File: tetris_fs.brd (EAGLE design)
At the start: 80.9 x 50.8 mm, 20 parts, among them IC1 78L24Z, U1 328P, Y1 16MHz

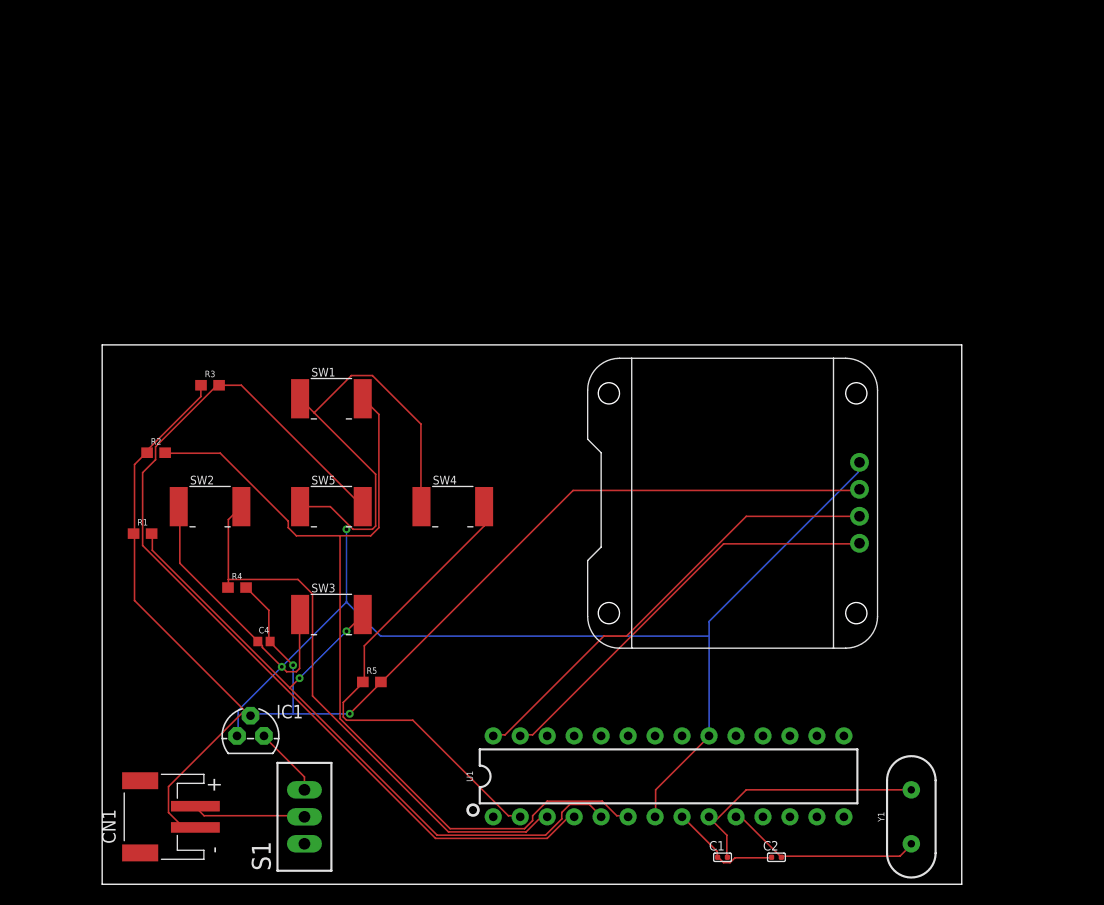
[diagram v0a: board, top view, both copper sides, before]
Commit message: Added full size resistor/capacitor version
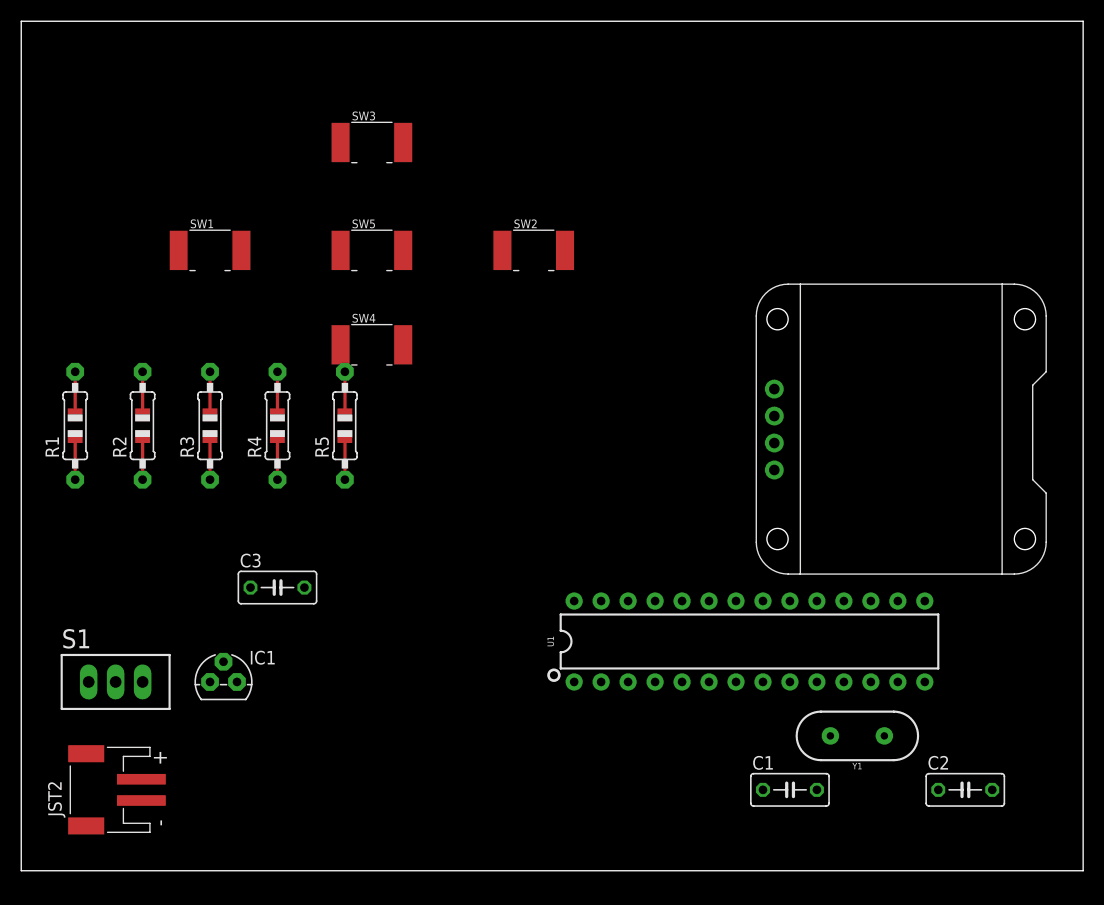
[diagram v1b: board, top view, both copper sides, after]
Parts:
- removed C4: 0.1uF, SparkFun-Capacitors:0402
- removed CN1: (no value), adafruit:JST-PH-2-SMT-RA
- added C3: 0.1uF, adafruit:C050-030X075
- added JST2: 1000mah 5V, adafruit:JST-PH-2-SMT-RA
- C1, C2: device Seeed-Capacitor:C0402 -> adafruit:C050-030X075
- R1, R2, R3, R4, R5: value 4.7k -> 1k; device SparkFun-Resistors:0603 -> adafruit:0805-THM
- moved SW3 44.6 mm to (33.0, 68.6)
- moved SW2 38.9 mm to (48.3, 58.4)
- moved SW5 24.4 mm to (33.0, 58.4)
- moved R5 24.3 mm to (30.5, 41.9), turned to 90 degrees
- moved FRAME1 22.2 mm to (-26.7, 74.9)
- moved S1 21.8 mm to (8.89, 17.8), turned to 0 degrees
- moved C2 18.9 mm to (88.9, 7.62), turned to 0 degrees
- moved SW1 18.1 mm to (17.8, 58.4)
- moved SW4 17.0 mm to (33.0, 49.5)
- moved U$1 17.0 mm to (82.5, 41.9), turned to 90 degrees
- moved R4 15.7 mm to (24.1, 41.9), turned to 90 degrees
- moved U1 14.8 mm to (68.6, 21.6)
- moved R1 12.0 mm to (5.08, 41.9), turned to 90 degrees
- moved Y1 9.16 mm to (78.7, 12.7), turned to 180 degrees
- moved C1 8.98 mm to (72.4, 7.62), turned to 0 degrees
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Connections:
- net GND: now also C3.2, JST2.2, R1.2, R2.2, R3.2; no longer C4.2, CN1.2, R1.1, R2.1, R3.1
- net N$1: no longer R2.2
- net N$2: now also R1.1; no longer R1.2
- net N$3: now also R3.1, R5.1; no longer R3.2
- net N$4: now also R2.1; no longer R4.1
- net N$5: now also R4.1; no longer R5.1
- net N$9: now also JST2.1; no longer CN1.1
- net VCC: now also C3.1; no longer C4.1
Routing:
- net VCC: track 171.6 -> 0.00 mm, vias 2 -> 0
- net GND: track 134.8 -> 0.00 mm, vias 2 -> 0
- net N$3: track 89.3 -> 0.00 mm
- net N$1: track 87.5 -> 0.00 mm
- net N$2: track 66.8 -> 0.00 mm, vias 2 -> 0
- net N$4: track 54.3 -> 0.00 mm
- net N$5: track 45.9 -> 0.00 mm
- net N$11: track 43.1 -> 0.00 mm
- net N$10: track 39.5 -> 0.00 mm
- net N$6: track 25.1 -> 0.00 mm
- net N$7: track 18.7 -> 0.00 mm
- net N$9: track 10.8 -> 0.00 mm
- net N$8: track 10.7 -> 0.00 mm
- net N$12: track 6.66 -> 0.00 mm
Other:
- board size 80.9 x 50.8 mm -> 100 x 80 mm

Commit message: updated board layout, updated readme
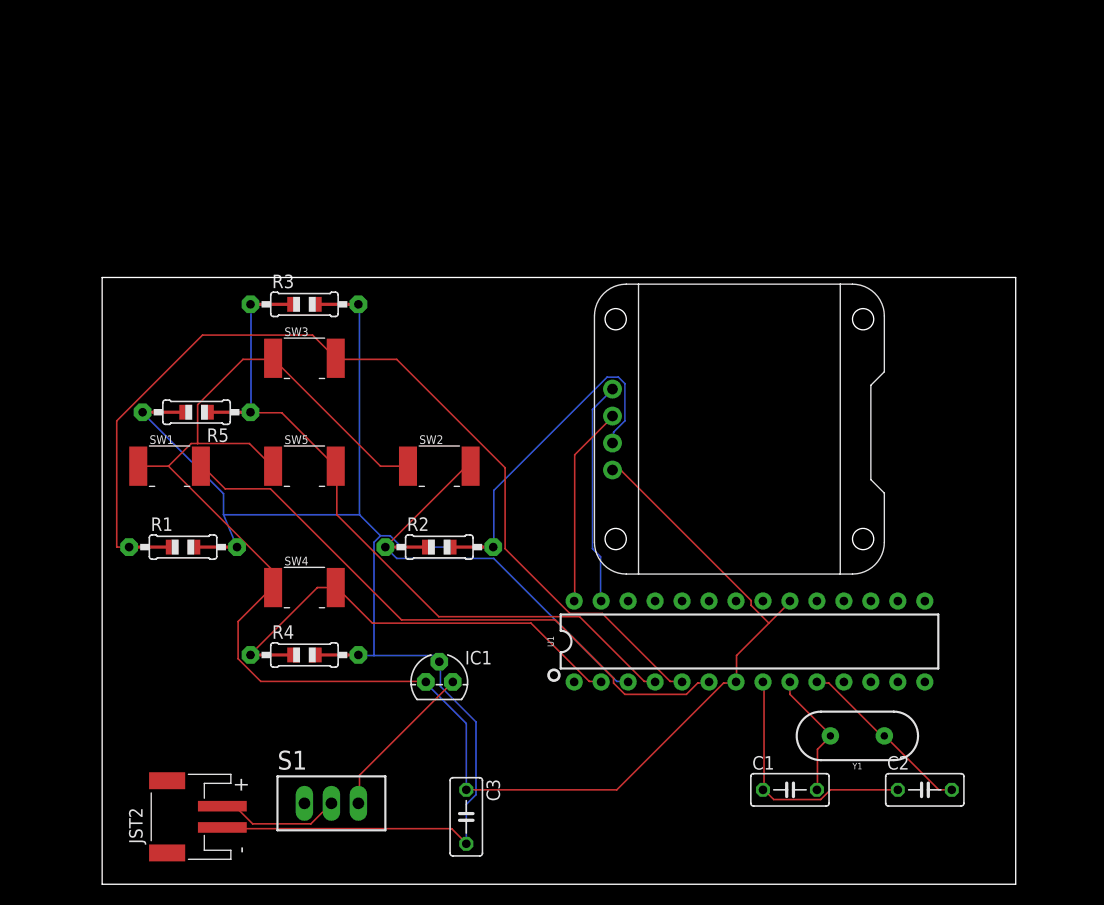
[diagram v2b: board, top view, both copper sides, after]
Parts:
- moved R2 30.2 mm to (39.4, 30.5), turned to 0 degrees
- moved C3 28.0 mm to (41.9, 5.08), turned to 270 degrees
- moved SW4 23.7 mm to (26.7, 26.7)
- moved S1 23.3 mm to (29.2, 6.35)
- moved SW2 22.2 mm to (39.4, 38.1)
- moved R4 21.7 mm to (26.7, 20.3), turned to 0 degrees
- moved SW3 21.3 mm to (26.7, 48.3)
- moved SW5 21.3 mm to (26.7, 38.1)
- moved SW1 20.7 mm to (14.0, 38.1)
- moved IC1 20.3 mm to (39.4, 17.8)
- moved R1 15.3 mm to (15.2, 30.5), turned to 0 degrees
- moved U$1 15.2 mm to (67.3, 41.9)
- moved R3 14.5 mm to (26.7, 53.3), turned to 0 degrees
- moved R5 14.0 mm to (16.5, 43.2), turned to 180 degrees
- moved JST2 8.03 mm to (15.2, 5.08)
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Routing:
- net VCC: track 0.00 -> 158.2 mm
- net GND: track 0.00 -> 153.2 mm
- net N$2: track 0.00 -> 87.6 mm
- net N$3: track 0.00 -> 61.5 mm
- net N$1: track 0.00 -> 57.6 mm
- net N$5: track 0.00 -> 39.4 mm
- net N$4: track 0.00 -> 39.3 mm
- net N$8: track 0.00 -> 23.7 mm
- net N$10: track 0.00 -> 21.1 mm
- net N$11: track 0.00 -> 18.9 mm
- net N$7: track 0.00 -> 16.9 mm
- net N$12: track 0.00 -> 15.1 mm
- net N$6: track 0.00 -> 12.3 mm
- net N$9: track 0.00 -> 11.8 mm
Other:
- board size 100 x 80 mm -> 86 x 57.1 mm
